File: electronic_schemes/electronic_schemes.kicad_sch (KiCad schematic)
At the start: 9 parts, among them M1 Motor_DC, Q1 AO3400A

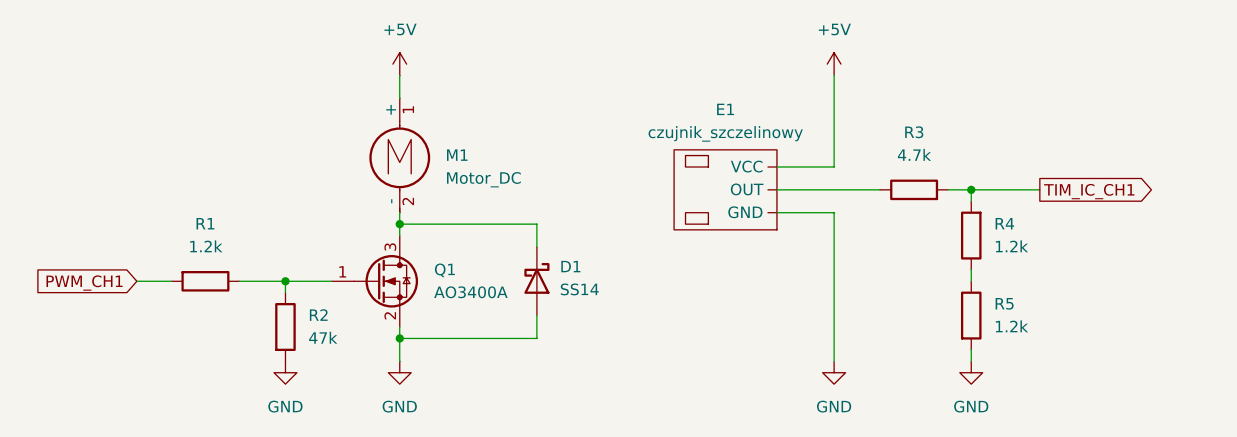
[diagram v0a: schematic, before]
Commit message: Entry schematics added
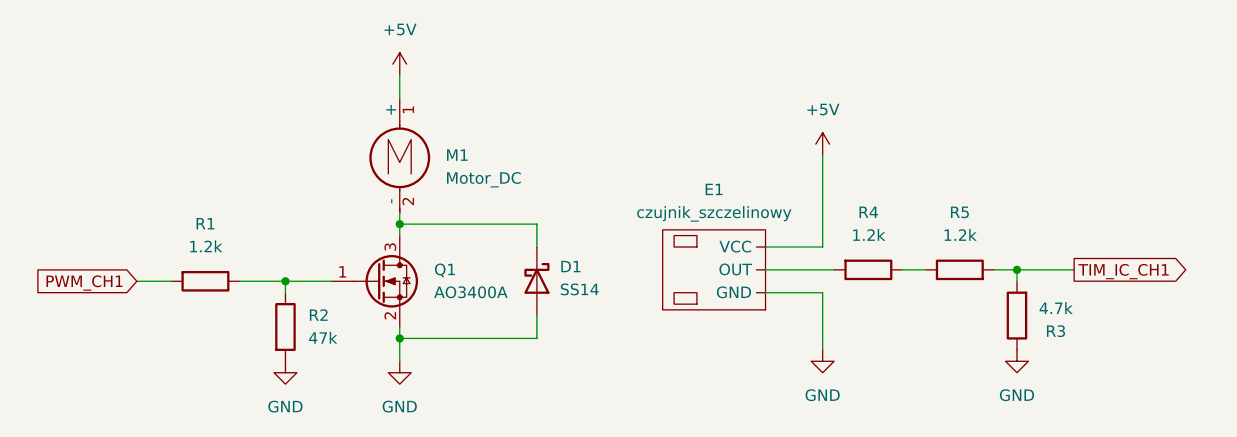
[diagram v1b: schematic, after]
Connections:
- net GND: now also R3.1; no longer R5.2
- net TIM_IC_CH1: now also R5.2; no longer R4.2
- new net: E1. (VCC), R4.2
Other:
- moved on the sheet: E1, R3, R4, R5
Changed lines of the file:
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@@
 	(paper "A4")
 	(junction
-		(at 139.7 71.12)
+		(at 144.78 80.01)
 		(diameter 0)
 		(color 0 0 0 0)
@@
 	(wire
 		(pts
-			(xy 139.7 71.12) (xy 147.32 71.12)
+			(xy 144.78 80.01) (xy 151.13 80.01)
 		)
 		(stroke
@@
 	(wire
 		(pts
-			(xy 124.46 58.42) (xy 124.46 68.58)
+			(xy 123.19 67.31) (xy 123.19 77.47)
 		)
 		(stroke
@@
 	(wire
 		(pts
-			(xy 139.7 88.9) (xy 139.7 90.17)
-		)
-		(stroke
-			(width 0)
-			(type default)
-		)
-	)
-	(wire
-		(pts
-			(xy 118.11 73.66) (xy 124.46 73.66)
-		)
-		(stroke
-			(width 0)
-			(type default)
-		)
-	)
-	(wire
-		(pts
-			(xy 118.11 68.58) (xy 124.46 68.58)
+			(xy 116.84 82.55) (xy 123.19 82.55)
+		)
+		(stroke
+			(width 0)
+			(type default)
+		)
+	)
+	(wire
+		(pts
+			(xy 116.84 77.47) (xy 123.19 77.47)
 		)
 		(stroke
@@
 	(wire
 		(pts
-			(xy 118.11 71.12) (xy 129.54 71.12)
+			(xy 116.84 80.01) (xy 124.46 80.01)
 		)
 		(stroke
@@
 	(wire
 		(pts
-			(xy 139.7 71.12) (xy 139.7 72.39)
-		)
-		(stroke
-			(width 0)
-			(type default)
-		)
-	)
-	(wire
-		(pts
-			(xy 137.16 71.12) (xy 139.7 71.12)
+			(xy 132.08 80.01) (xy 134.62 80.01)
+		)
+		(stroke
+			(width 0)
+			(type default)
+		)
+	)
+	(wire
+		(pts
+			(xy 144.78 80.01) (xy 144.78 81.28)
+		)
+		(stroke
+			(width 0)
+			(type default)
+		)
+	)
+	(wire
+		(pts
+			(xy 142.24 80.01) (xy 144.78 80.01)
 		)
 		(stroke
@@
 	(wire
 		(pts
-			(xy 124.46 90.17) (xy 124.46 73.66)
+			(xy 123.19 88.9) (xy 123.19 82.55)
 		)
 		(stroke
@@
 		(pts
 			(xy 46.99 81.28) (xy 50.8 81.28)
-		)
-		(stroke
-			(width 0)
-			(type default)
-		)
-	)
-	(wire
-		(pts
-			(xy 139.7 80.01) (xy 139.7 81.28)
 		)
 		(stroke
@@
 	(global_label "TIM_IC_CH1"
 		(shape output)
-		(at 147.32 71.12 0)
+		(at 151.13 80.01 0)
 		(fields_autoplaced yes)
 		(effects
@@
 		)
 		(property "Intersheetrefs" "${INTERSHEET_REFS}"
-			(at 160.949 71.12 0)
+			(at 164.759 80.01 0)
 			(effects
 				(font
@@
 	(symbol
 		(lib_id "power:+5V")
-		(at 124.46 58.42 0)
+		(at 123.19 67.31 0)
 		(unit 1)
 		(exclude_from_sim no)
@@
 		(fields_autoplaced yes)
 		(property "Reference" "#PWR04"
-			(at 124.46 62.23 0)
+			(at 123.19 71.12 0)
 			(effects
 				(font
@@
 		)
 		(property "Value" "+5V"
-			(at 124.46 53.34 0)
+			(at 123.19 62.23 0)
 			(effects
 				(font
@@
 		)
 		(property "Footprint" ""
-			(at 124.46 58.42 0)
+			(at 123.19 67.31 0)
 			(effects
 				(font
@@
 		)
 		(property "Datasheet" ""
-			(at 124.46 58.42 0)
+			(at 123.19 67.31 0)
 			(effects
 				(font
@@
 		)
 		(property "Description" "Power symbol creates a global label with name \"+5V\""
-			(at 124.46 58.42 0)
+			(at 123.19 67.31 0)
 			(effects
 				(font
@@
 	(symbol
 		(lib_id "power:GND")
-		(at 124.46 90.17 0)
+		(at 123.19 88.9 0)
 		(unit 1)
 		(exclude_from_sim no)
@@
 		(fields_autoplaced yes)
 		(property "Reference" "#PWR05"
-			(at 124.46 96.52 0)
+			(at 123.19 95.25 0)
 			(effects
 				(font
@@
 		)
 		(property "Value" "GND"
-			(at 124.46 95.25 0)
+			(at 123.19 93.98 0)
 			(effects
 				(font
@@
 		)
 		(property "Footprint" ""
-			(at 124.46 90.17 0)
+			(at 123.19 88.9 0)
 			(effects
 				(font
@@
 		)
 		(property "Datasheet" ""
-			(at 124.46 90.17 0)
+			(at 123.19 88.9 0)
 			(effects
 				(font
@@
 		)
 		(property "Description" "Power symbol creates a global label with name \"GND\" , ground"
-			(at 124.46 90.17 0)
+			(at 123.19 88.9 0)
 			(effects
 				(font
@@
 	(symbol
 		(lib_id "power:GND")
-		(at 139.7 90.17 0)
+		(at 144.78 88.9 0)
 		(unit 1)
 		(exclude_from_sim no)
@@
 		(fields_autoplaced yes)
 		(property "Reference" "#PWR06"
-			(at 139.7 96.52 0)
+			(at 144.78 95.25 0)
 			(effects
 				(font
@@
 		)
 		(property "Value" "GND"
-			(at 139.7 95.25 0)
+			(at 144.78 93.98 0)
 			(effects
 				(font
@@
 		)
 		(property "Footprint" ""
-			(at 139.7 90.17 0)
+			(at 144.78 88.9 0)
 			(effects
 				(font
@@
 		)
 		(property "Datasheet" ""
-			(at 139.7 90.17 0)
+			(at 144.78 88.9 0)
 			(effects
 				(font
@@
 		)
 		(property "Description" "Power symbol creates a global label with name \"GND\" , ground"
-			(at 139.7 90.17 0)
+			(at 144.78 88.9 0)
 			(effects
 				(font
@@
 	(symbol
 		(lib_id "Device:R")
-		(at 139.7 85.09 0)
+		(at 138.43 80.01 90)
 		(unit 1)
 		(exclude_from_sim no)
@@
 		(fields_autoplaced yes)
 		(property "Reference" "R5"
-			(at 142.24 83.8199 0)
-			(effects
-				(font
-					(size 1.27 1.27)
-				)
-				(justify left)
+			(at 138.43 73.66 90)
+			(effects
+				(font
+					(size 1.27 1.27)
+				)
 			)
 		)
 		(property "Value" "1.2k"
-			(at 142.24 86.3599 0)
-			(effects
-				(font
-					(size 1.27 1.27)
-				)
-				(justify left)
+			(at 138.43 76.2 90)
+			(effects
+				(font
+					(size 1.27 1.27)
+				)
 			)
 		)
 		(property "Footprint" ""
-			(at 137.922 85.09 90)
+			(at 138.43 81.788 90)
 			(effects
 				(font
@@
 		)
 		(property "Datasheet" "~"
-			(at 139.7 85.09 0)
+			(at 138.43 80.01 0)
 			(effects
 				(font
@@
 		)
 		(property "Description" "Resistor"
-			(at 139.7 85.09 0)
+			(at 138.43 80.01 0)
 			(effects
 				(font
@@
 		)
 		(instances
-			(project ""
+			(project "electronic_schemes"
 				(path "/bd3ac37f-2034-4619-be04-000bef16974b"
 					(reference "R5")
@@
 	(symbol
 		(lib_id "New_Library:Enkoder")
-		(at 110.49 71.12 180)
+		(at 109.22 80.01 180)
 		(unit 1)
 		(exclude_from_sim no)
@@
 		(fields_autoplaced yes)
 		(property "Reference" "E1"
-			(at 112.395 62.23 0)
+			(at 111.125 71.12 0)
 			(effects
 				(font
@@
 		)
 		(property "Value" "czujnik_szczelinowy"
-			(at 112.395 64.77 0)
+			(at 111.125 73.66 0)
 			(effects
 				(font
@@
 		)
 		(property "Footprint" ""
-			(at 110.49 71.12 0)
+			(at 109.22 80.01 0)
 			(effects
 				(font
@@
 		)
 		(property "Datasheet" ""
-			(at 110.49 71.12 0)
+			(at 109.22 80.01 0)
 			(effects
 				(font
@@
 		)
 		(property "Description" ""
-			(at 110.49 71.12 0)
+			(at 109.22 80.01 0)
 			(effects
 				(font
@@
 	(symbol
 		(lib_id "Device:R")
-		(at 139.7 76.2 180)
+		(at 128.27 80.01 270)
 		(unit 1)
 		(exclude_from_sim no)
@@
 		(fields_autoplaced yes)
 		(property "Reference" "R4"
-			(at 142.24 74.9299 0)
-			(effects
-				(font
-					(size 1.27 1.27)
-				)
-				(justify right)
+			(at 128.27 73.66 90)
+			(effects
+				(font
+					(size 1.27 1.27)
+				)
 			)
 		)
 		(property "Value" "1.2k"
-			(at 142.24 77.4699 0)
-			(effects
-				(font
-					(size 1.27 1.27)
-				)
-				(justify right)
+			(at 128.27 76.2 90)
+			(effects
+				(font
+					(size 1.27 1.27)
+				)
 			)
 		)
 		(property "Footprint" ""
-			(at 141.478 76.2 90)
+			(at 128.27 78.232 90)
 			(effects
 				(font
@@
 		)
 		(property "Datasheet" "~"
-			(at 139.7 76.2 0)
+			(at 128.27 80.01 0)
 			(effects
 				(font
@@
 		)
 		(property "Description" "Resistor"
-			(at 139.7 76.2 0)
+			(at 128.27 80.01 0)
 			(effects
 				(font
@@
 		)
 		(instances
-			(project ""
+			(project "electronic_schemes"
 				(path "/bd3ac37f-2034-4619-be04-000bef16974b"
 					(reference "R4")
@@
 	(symbol
 		(lib_id "Device:R")
-		(at 133.35 71.12 90)
+		(at 144.78 85.09 180)
 		(unit 1)
 		(exclude_from_sim no)
@@
 		(dnp no)
 		(property "Reference" "R3"
-			(at 133.35 64.77 90)
+			(at 149.098 86.868 0)
 			(effects
 				(font
@@
 		)
 		(property "Value" "4.7k"
-			(at 133.35 67.31 90)
+			(at 149.098 84.328 0)
 			(effects
 				(font
@@
 		)
 		(property "Footprint" ""
-			(at 133.35 72.898 90)
+			(at 146.558 85.09 90)
 			(effects
 				(font
@@
 		)
 		(property "Datasheet" "~"
-			(at 133.35 71.12 0)
+			(at 144.78 85.09 0)
 			(effects
 				(font
@@
 		)
 		(property "Description" "Resistor"
-			(at 133.35 71.12 0)
-			(effects
-				(font
+			(at 144.78 85.09 0)
+			(effects
+				(font
